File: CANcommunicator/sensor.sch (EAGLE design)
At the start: 31 parts, among them U1 ATSAMC21E18A-AU, U2 MCP2551

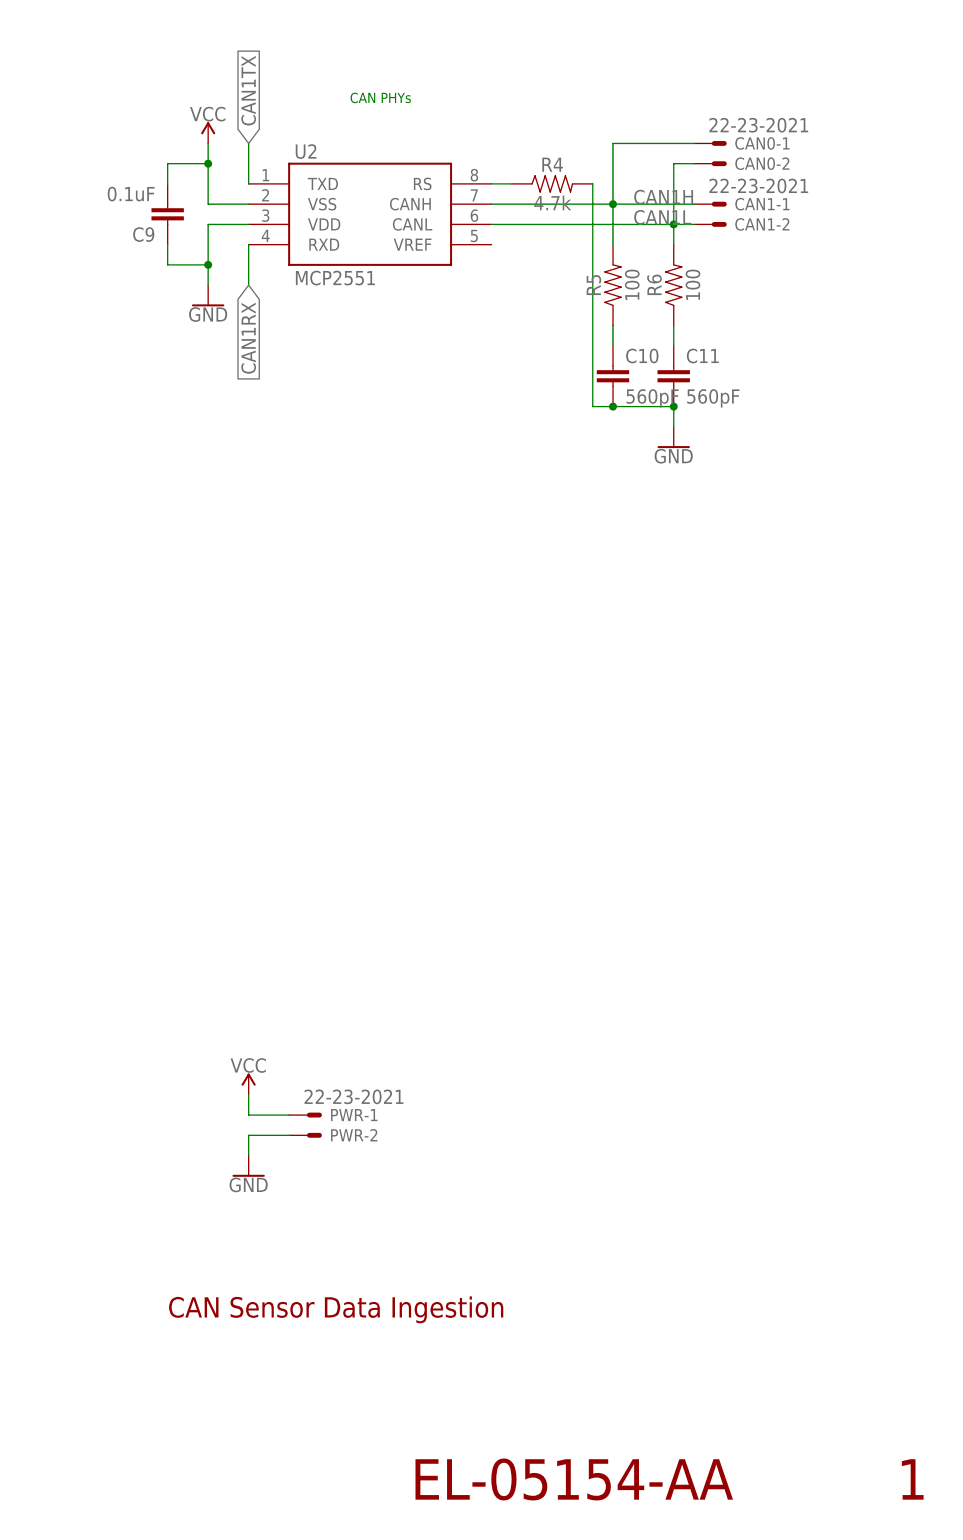
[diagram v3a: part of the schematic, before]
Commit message: Fix insanely obvious error in CAN interface
VSS means GROUND, VDD means POWER
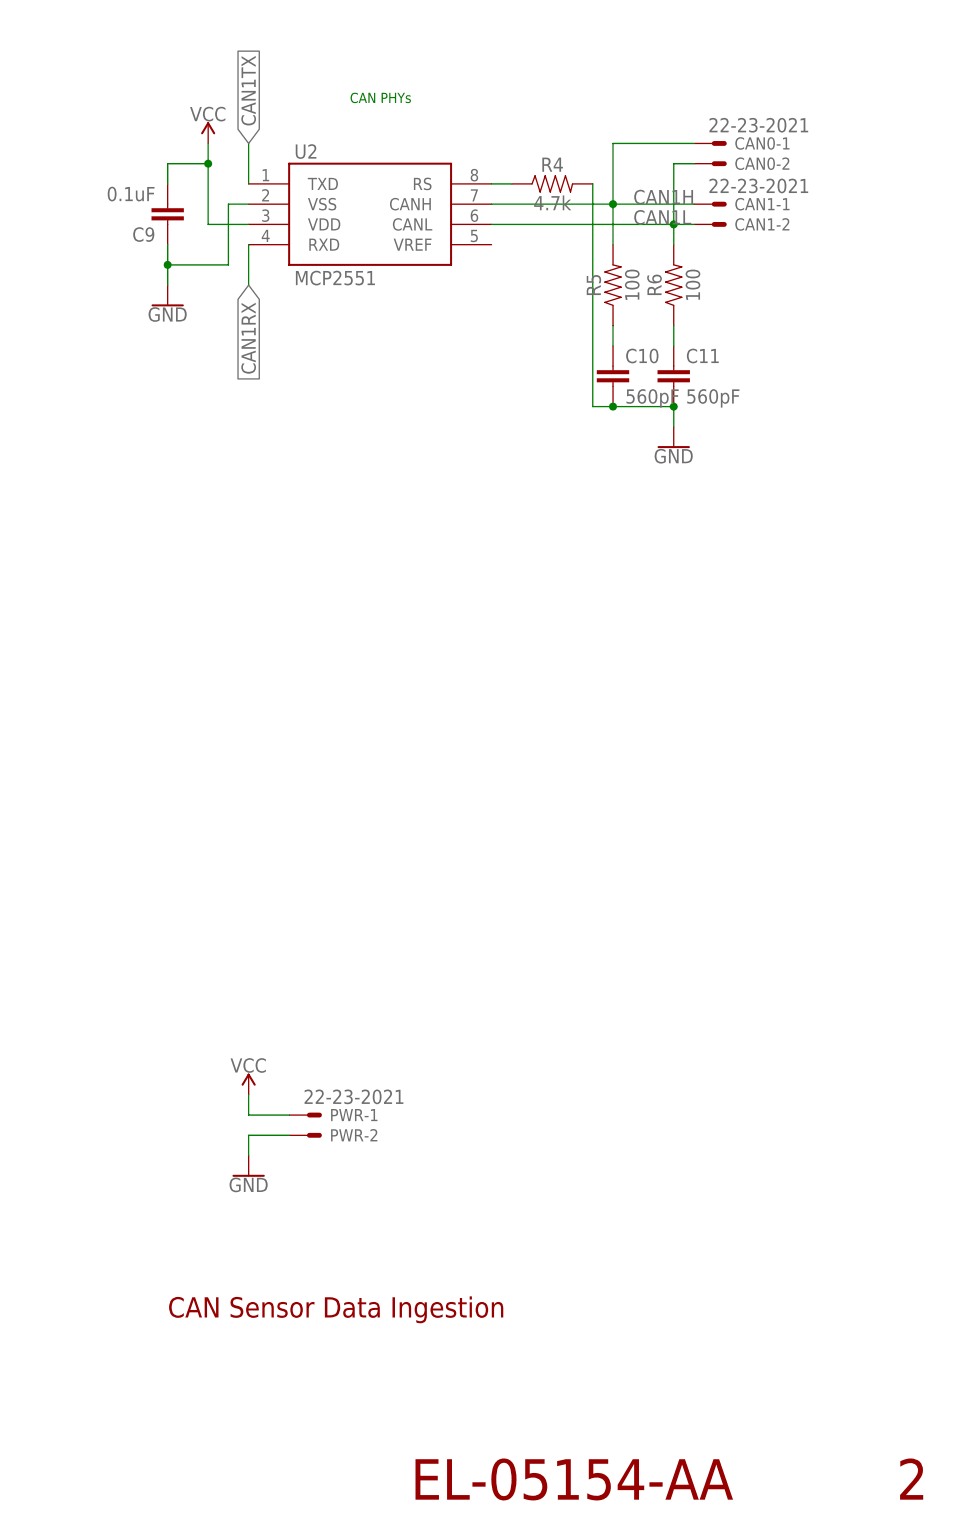
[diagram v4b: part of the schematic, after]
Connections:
- net GND: now also U2.VSS; no longer U2.VDD
- net VCC: now also U2.VDD; no longer U2.VSS
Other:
- note added: "2"
- note removed: "1"
